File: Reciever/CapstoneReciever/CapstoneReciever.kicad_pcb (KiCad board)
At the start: 2 copper layers, 70 parts, among them J1 Conn_01x04, J2 Conn_01x04, J3 Sol1Conn, J4 Sol2Conn, J5 Sol3Conn, J6 Sol4Conn, Q1 CSD18502Q5B, Q2 CSD18502Q5B, Q3 CSD18540Q5B, Q4 CSD18540Q5B, Q5 CSD18540Q5B, Q6 CSD18540Q5B, U1 LM73606RNPR, U2 TPS552882RPMR, U3 ESP32-WROOM-32UE

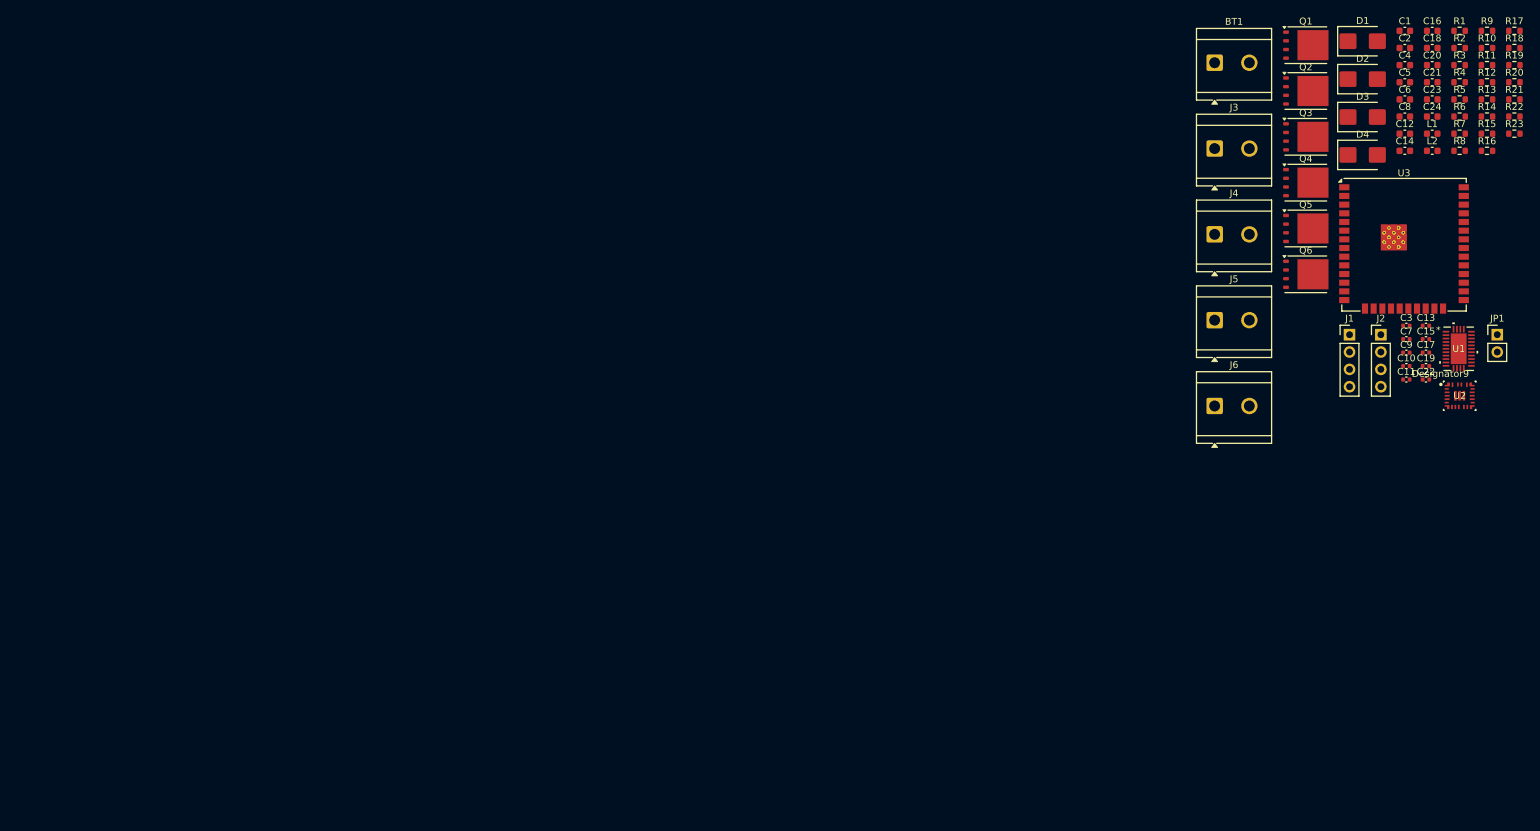
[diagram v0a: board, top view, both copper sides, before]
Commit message: Added more descriptive net names and routed low side switching mosfets with ESP32 decoupling
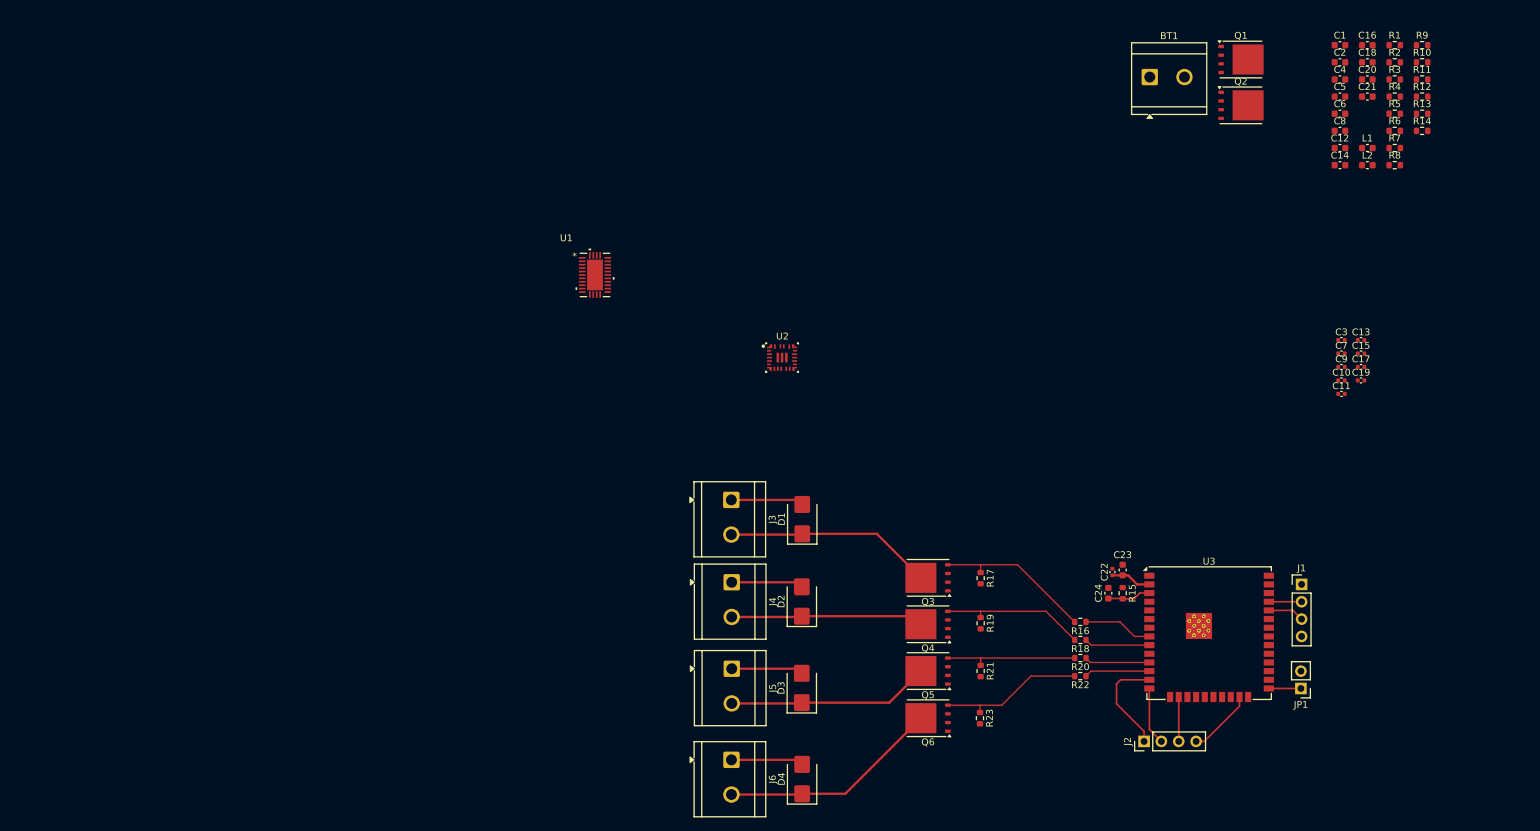
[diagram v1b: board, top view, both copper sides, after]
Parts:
- moved U1 126.9 mm to (132.0, 68.5)
- moved D4 122.8 mm to (162.4, 142.3), turned to 90 degrees
- moved D3 117.2 mm to (162.3, 129.0), turned to 90 degrees
- moved R23 116.0 mm to (188.4, 133.4), turned to -90 degrees
- moved R21 114.5 mm to (188.5, 126.5), turned to -90 degrees
- moved R19 113.1 mm to (188.5, 119.5), turned to -90 degrees
- moved D2 112.2 mm to (162.3, 116.3), turned to 90 degrees
- moved R17 111.9 mm to (188.5, 112.9), turned to -90 degrees
- moved D1 107.9 mm to (162.4, 104.3), turned to 90 degrees
- moved R18 107.5 mm to (203.1, 122.0), turned to 180 degrees
- moved R20 105.6 mm to (203.1, 124.6), turned to 180 degrees
- moved R22 103.7 mm to (203.1, 127.2), turned to 180 degrees
- moved U2 99.4 mm to (159.4, 80.6)
- moved R16 91.1 mm to (203.1, 119.3), turned to 180 degrees
- moved J6 87.7 mm to (152.0, 139.5), turned to -90 degrees
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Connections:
- net Net-(J3-Pin_2) renamed /Q3Drain
- net Net-(J4-Pin_2) renamed /Q4Drain
- net Net-(J5-Pin_2) renamed /Q5Drain
- net Net-(J6-Pin_2) renamed /Q6Drain
- net Net-(Q3-G) renamed /Q3Gate
- net Net-(Q4-G) renamed /Q4Gate
- net Net-(Q5-G) renamed /Q5Gate
- net Net-(Q6-G) renamed /Q6Gate
- U3 pad 11: /Solenoid4Gate -> /Solenoid3Gate
- U3 pad 12: /Solenoid3Gate -> /Solenoid4Gate
- U3 pad 8: /Solenoid2Gate -> /Solenoid1Gate
- U3 pad 9: /Solenoid1Gate -> /Solenoid2Gate
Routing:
- net +12V: track 0.00 -> 42.4 mm
- net /Q6Drain: track 0.00 -> 32.4 mm
- net /Q3Drain: track 0.00 -> 30.5 mm
- net /Q5Drain: track 0.00 -> 29.7 mm
- net /Q4Drain: track 0.00 -> 28.2 mm
- net /Q3Gate: track 0.00 -> 23.2 mm
- net /Q6Gate: track 0.00 -> 21.4 mm
- net /Q4Gate: track 0.00 -> 21.2 mm
- net /Q5Gate: track 0.00 -> 19.7 mm
- net /JTAG_TMS: track 0.00 -> 15.1 mm
- net /Solenoid1Gate: track 0.00 -> 10.2 mm
- net /JTAG_TDO: track 0.00 -> 9.83 mm
- net /Solenoid2Gate: track 0.00 -> 9.59 mm
- net /Solenoid4Gate: track 0.00 -> 9.58 mm
- net /Solenoid3Gate: track 0.00 -> 9.55 mm
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
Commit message: Attempted to work on power routing. Stuck. Please assist
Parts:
- moved U2 113.0 mm to (49.2, 55.9), turned to 90 degrees
- moved U1 84.9 mm to (49.8, 47.6), turned to 180 degrees
- moved L1 3.32 mm to (245.0, 46.6)
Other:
- copper layers 2 -> 4

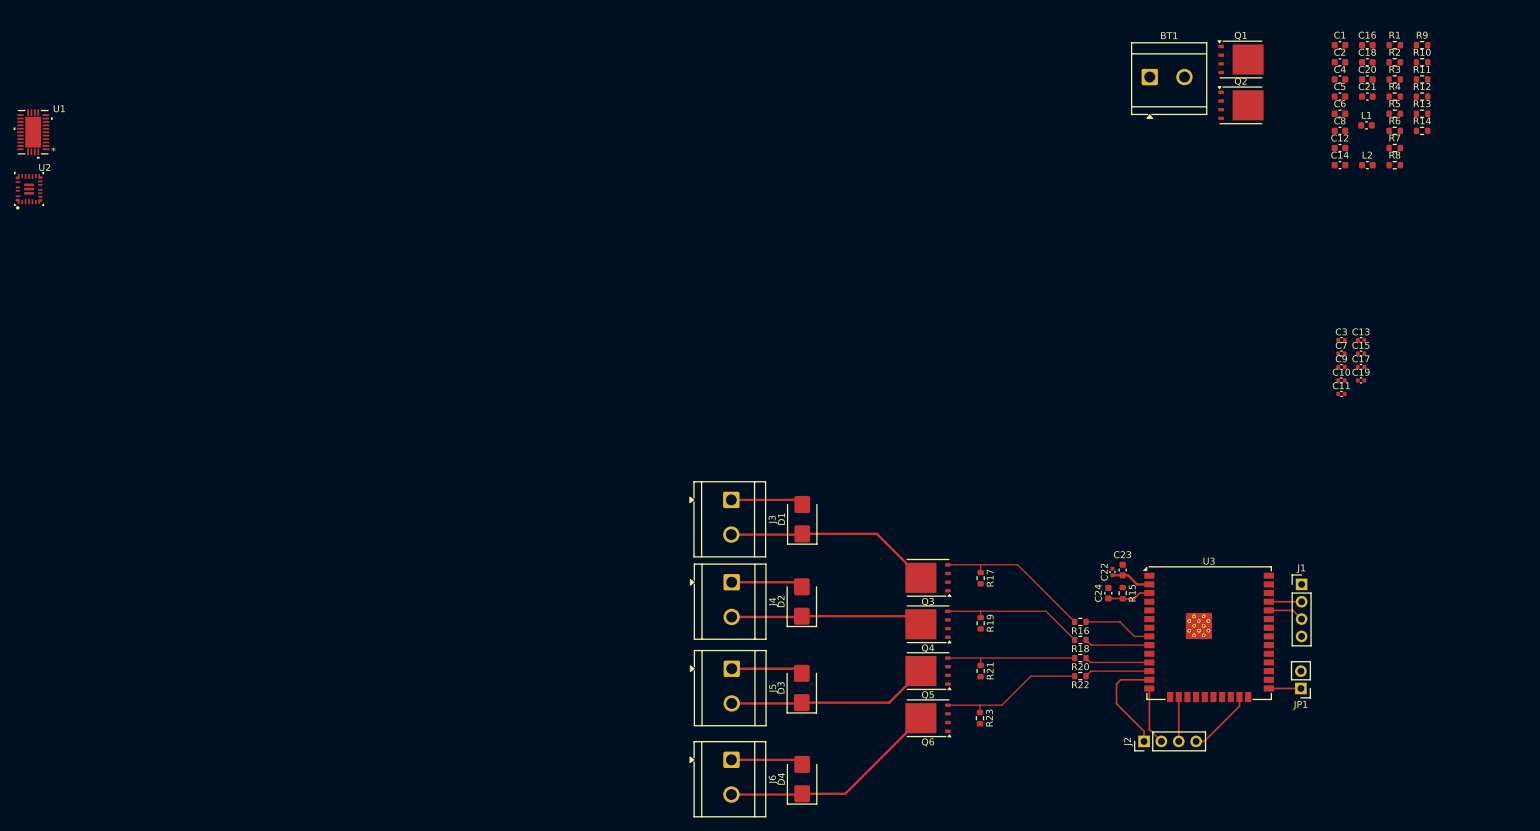
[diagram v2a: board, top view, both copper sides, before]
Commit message: Removed convoluted battery power routing in exchange of DIN mounted AC-DC converter and DC-DC converter inputs
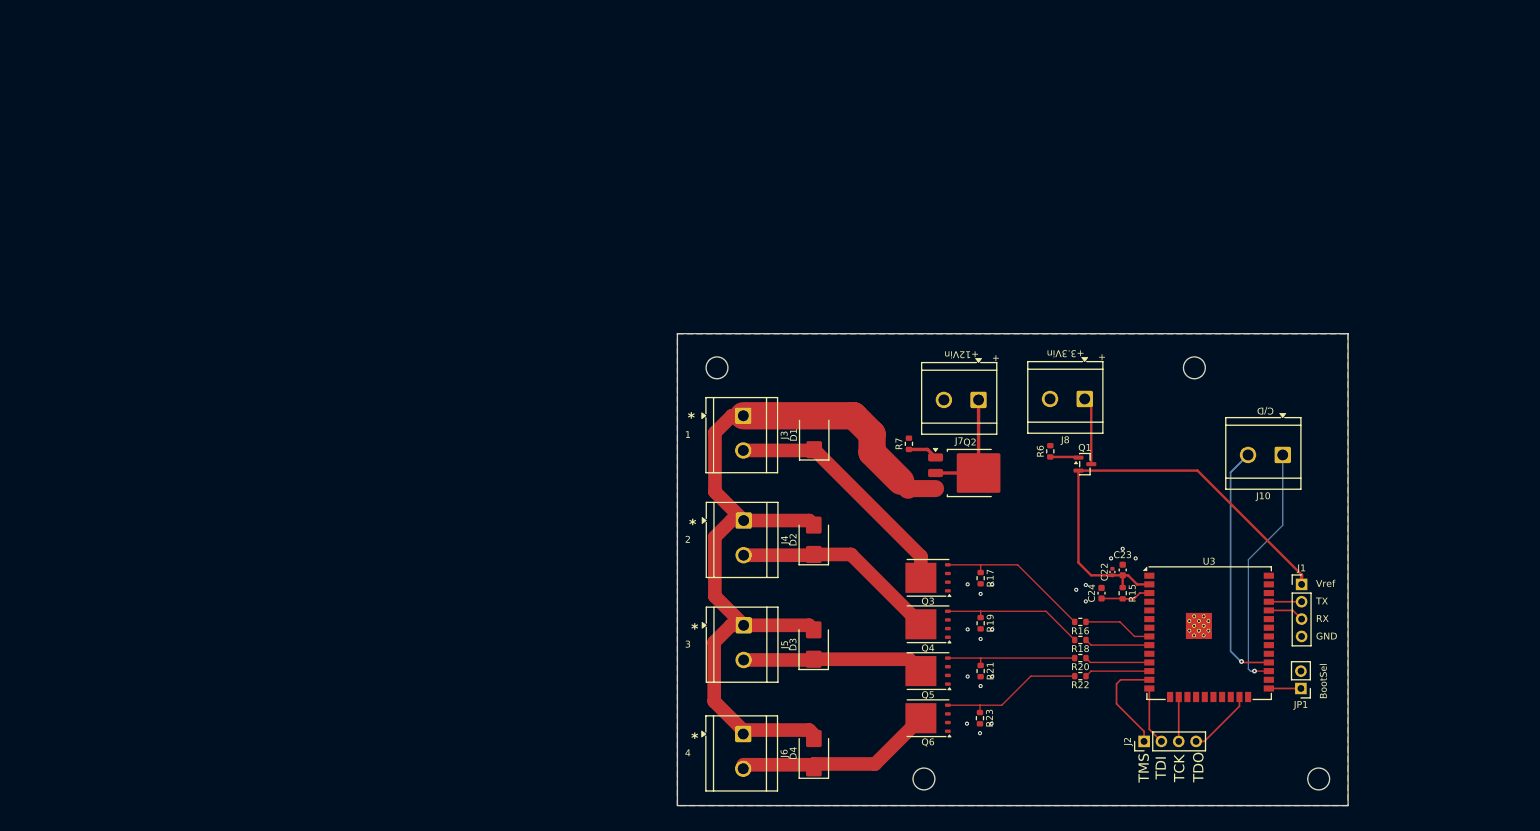
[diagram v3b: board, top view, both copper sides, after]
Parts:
- removed BT1: Battery, TerminalBlock_CUI:TerminalBlock_CUI_TB007-508-02_1x02_P5.08mm_Horizontal
- removed C1, C4, C6: 100u, Capacitor_SMD:C_0603_1608Metric
- removed C10, C7: 470n, Capacitor_SMD:C_0402_1005Metric
- removed C11, C13: 100n, Capacitor_SMD:C_0402_1005Metric
- removed C12: 22u, Capacitor_SMD:C_0603_1608Metric
- removed C14, C16, C20, C8: 10u, Capacitor_SMD:C_0603_1608Metric
- removed C15: 10n, Capacitor_SMD:C_0402_1005Metric
- removed C17: 15p, Capacitor_SMD:C_0402_1005Metric
- removed C18: 150u, Capacitor_SMD:C_0603_1608Metric
- removed C19: 47n, Capacitor_SMD:C_0402_1005Metric
- removed C2, C5: 68u, Capacitor_SMD:C_0603_1608Metric
- removed C21: 4u7, Capacitor_SMD:C_0603_1608Metric
- removed C3, C9: 43p, Capacitor_SMD:C_0402_1005Metric
- removed L1: 3u3, Capacitor_SMD:C_0603_1608Metric
- removed L2: 8u2, Capacitor_SMD:C_0603_1608Metric
- removed R1, R13, R3, R4, R5: 100k, Resistor_SMD:R_0603_1608Metric
- removed R10, R9: 1, Resistor_SMD:R_0603_1608Metric
- removed R11: 35k, Resistor_SMD:R_0603_1608Metric
- removed R12: 16k, Resistor_SMD:R_0603_1608Metric
- removed R14: 11k, Resistor_SMD:R_0603_1608Metric
- removed R2: 43.5k, Resistor_SMD:R_0603_1608Metric
- removed R8: 50k, Resistor_SMD:R_0603_1608Metric
- removed U1: LM73606RNPR, footprints2:RNP30_TEX
- removed U2: TPS552882RPMR, footprints2:RPM0026A-MFG
- added J10: C/D, TerminalBlock_CUI:TerminalBlock_CUI_TB007-508-02_1x02_P5.08mm_Horizontal, F.Cu at (232.7, 94.9)
- added J7: +12Vin, TerminalBlock_CUI:TerminalBlock_CUI_TB007-508-02_1x02_P5.08mm_Horizontal, F.Cu at (188.2, 86.8)
- added J8: +3.3Vin, TerminalBlock_CUI:TerminalBlock_CUI_TB007-508-02_1x02_P5.08mm_Horizontal, F.Cu at (203.7, 86.7)
- added REF**: MountingHole_3.2mm_M3_ISO7380, MountingHole:MountingHole_3.2mm_M3_ISO7380, F.Cu at (238.0, 142.3)
- added REF**: MountingHole_3.2mm_M3_ISO7380, MountingHole:MountingHole_3.2mm_M3_ISO7380, F.Cu at (149.9, 82.1)
- added REF**: MountingHole_3.2mm_M3_ISO7380, MountingHole:MountingHole_3.2mm_M3_ISO7380, F.Cu at (180.2, 142.3)
- added REF**: MountingHole_3.2mm_M3_ISO7380, MountingHole:MountingHole_3.2mm_M3_ISO7380, F.Cu at (219.8, 82.1)
- Q1: value CSD18502Q5B -> DMP2035U; footprint Package_TO_SOT_SMD:TDSON-8-1 -> Package_TO_SOT_SMD:SOT-23
- Q2: value CSD18502Q5B -> SQD50P04-09L; footprint Package_TO_SOT_SMD:TDSON-8-1 -> Package_TO_SOT_SMD:TO-252-3_TabPin2
- R6: value 635k -> 100K
- R7: value 100k -> 100K
- moved R7 83.3 mm to (178.0, 93.2), turned to 90 degrees
- moved R6 68.9 mm to (198.7, 94.3), turned to 90 degrees
- moved Q2 66.9 mm to (186.9, 97.5)
- moved Q1 63.5 mm to (203.8, 96.2)
- moved D1 12.4 mm to (164.1, 91.9)
- moved J3 12.4 mm to (153.7, 89.1)
- moved J4 9.21 mm to (153.8, 104.5)
- moved D2 9.21 mm to (164.1, 107.3)
- moved J5 6.59 mm to (153.8, 119.8)
- moved D3 6.59 mm to (164.1, 122.6)
- moved J6 4.15 mm to (153.7, 135.7)
- moved D4 4.15 mm to (164.1, 138.5)
- moved C24 1.00 mm to (206.2, 115.1)
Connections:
- Q1 pad 1: Net-(Q2-D) -> Net-(Q1-G)
- Q1 pad 2: Net-(Q2-D) -> +3.3V
- Q1 pad 3: Net-(Q2-D) -> Net-(J8-Pin_1)
- Q2 pad 1: GND -> Net-(Q2-G)
- Q2 pad 2: GND -> Net-(J7-Pin_1)
- Q2 pad 3: GND -> +12V
- R6 pad 1: +BATT -> Net-(Q1-G)
- R6 pad 2: Net-(U2-EN) -> GND
- R7 pad 1: Net-(U2-CC_N) -> Net-(Q2-G)
- R7 pad 2: /Vcc -> GND
- U3 pad 27: unconnected-(U3-IO16-Pad27) -> /DIR/C
- U3 pad 28: unconnected-(U3-IO17-Pad28) -> /PWM/D
- U3 pad 6: /DIR/C -> unconnected-(U3-IO34-Pad6)
- U3 pad 7: /PWM/D -> unconnected-(U3-IO35-Pad7)
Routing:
- net +12V: track 42.4 -> 125.2 mm
- net +3.3V: track 5.96 -> 67.4 mm
- net /DIR/C: track 0.00 -> 36.6 mm, vias 0 -> 1
- net /PWM/D: track 0.00 -> 36.1 mm, vias 0 -> 1
- net Net-(J7-Pin_1): track 0.00 -> 17.0 mm
- net Net-(J8-Pin_1): track 0.00 -> 9.94 mm
- net /Q3Drain: track 30.5 -> 35.7 mm
- net Net-(Q2-G): track 0.00 -> 4.38 mm
- net Net-(Q1-G): track 0.00 -> 4.17 mm
- net /Q4Drain: track 28.2 -> 31.9 mm
- net /Q6Drain: track 32.4 -> 28.8 mm
- net /Q5Drain: track 29.7 -> 26.7 mm
- net /EN: track 6.38 -> 7.38 mm
- net GND: vias 0 -> 18
- added copper zone on B.Cu, net GND
- added copper zone on F.Cu, net GND
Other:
- board outline added: 98.2 x 69.1 mm
- board text added: "*"
- board text added: "+"
- board text added: "1"
- board text added: "2"
- board text added: "3"
- board text added: "4"
- board text added: "BootSel"
- board text added: "GND"
- board text added: "RX"
- board text added: "TCK"
- board text added: "TDI"
- board text added: "TDO"
- board text added: "TMS"
- board text added: "TX"
- board text added: "Vref"
